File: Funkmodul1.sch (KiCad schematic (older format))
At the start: 14 parts, among them IC1 74HC4050, U1 ATMEGA128-16AU, Y1 Crystal_GND23

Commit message: Adds new submodules
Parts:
- removed IC1: 74HC4050, Housings_SSOP:SSOP-16_5.3x6.2mm_Pitch0.65mm, symbol 74HC4050
- removed R2, R3: R, Resistors_SMD:R_0603_HandSoldering, symbol R
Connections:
- net labels added: RX, TX
- net labels removed: +3V3, +5V, MISO, MOSI, SCK, SS
- wire segments 36 -> 23

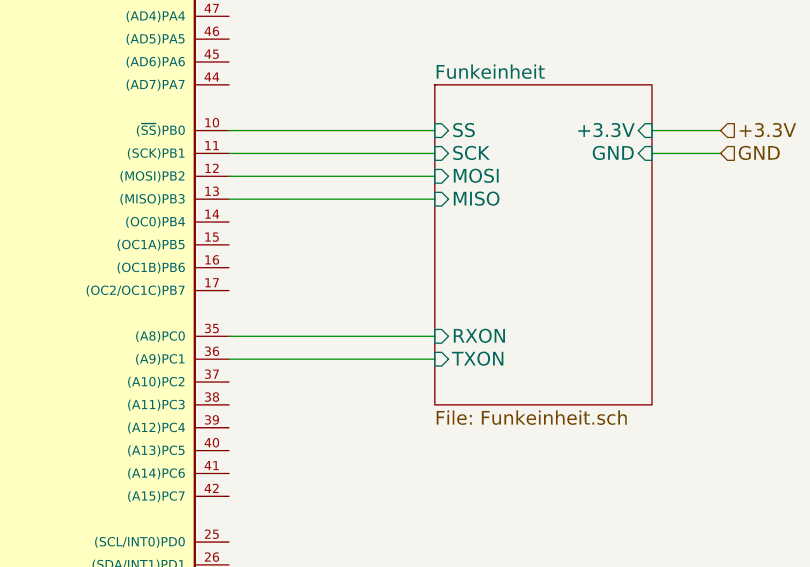
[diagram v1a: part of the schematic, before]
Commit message: Implements stepup dc/dc
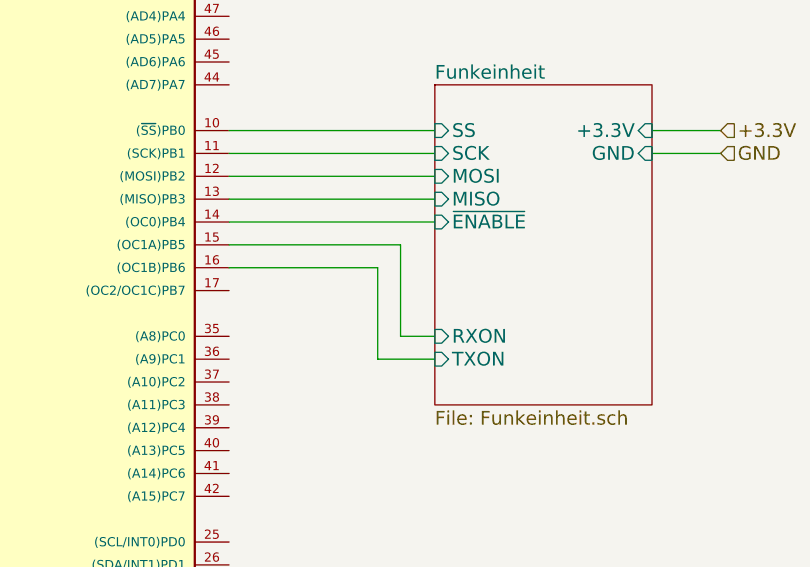
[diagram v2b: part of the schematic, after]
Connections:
- net Funkeinheit/RXON: now also U1.15 ((OC1A)PB5); no longer U1.35 ((A8)PC0)
- net Funkeinheit/TXON: now also U1.16 ((OC1B)PB6); no longer U1.36 ((A9)PC1)
- net Funkeinheit/~ENABLE~: now reaches U1.14 ((OC0)PB4)
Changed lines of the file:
@@
 LIBS:contrib
 LIBS:valves
+LIBS:nxp-ic
+LIBS:7400-ic
 LIBS:cubesatFunkmodul-cache
+LIBS:funkmodul
 EELAYER 25 0
 EELAYER END
@@
 U 1 1 59937F4F
 P 6850 3700
-AR Path="/5993797A/59937F4F" Ref="U1"  Part="1"
-AR Path="/5994EEB4/59937F4F" Ref="U2"  Part="1"
 F 0 "U1" H 5700 5600 50  0000 L BNN
 F 1 "ATMEGA128-16AU" H 7600 1750 50  0000 L BNN
@@
 U 1 1 59937F57
 P 6200 1300
-AR Path="/5993797A/59937F57" Ref="C4"  Part="1"
-AR Path="/5994EEB4/59937F57" Ref="C10"  Part="1"
 F 0 "C4" H 6225 1400 50  0000 L CNN
 F 1 "100nF" H 6225 1200 50  0000 L CNN
@@
 U 1 1 59937F5E
 P 6500 1300
-AR Path="/5993797A/59937F5E" Ref="C5"  Part="1"
-AR Path="/5994EEB4/59937F5E" Ref="C11"  Part="1"
 F 0 "C5" H 6525 1400 50  0000 L CNN
 F 1 "100nF" H 6525 1200 50  0000 L CNN
@@
 U 1 1 59937F89
 P 6850 1450
-AR Path="/5993797A/59937F89" Ref="L1"  Part="1"
-AR Path="/5994EEB4/59937F89" Ref="L2"  Part="1"
 F 0 "L1" V 6700 1475 50  0000 C CNN
 F 1 "10nH" V 7000 1450 50  0000 C CNN
@@
 U 1 1 59937F90
 P 7000 1250
-AR Path="/5993797A/59937F90" Ref="C6"  Part="1"
-AR Path="/5994EEB4/59937F90" Ref="C12"  Part="1"
 F 0 "C6" H 7025 1350 50  0000 L CNN
 F 1 "100nF" H 7025 1150 50  0000 L CNN
@@
 U 1 1 59937FF2
 P 5000 1850
-AR Path="/5993797A/59937FF2" Ref="R1"  Part="1"
-AR Path="/5994EEB4/59937FF2" Ref="R4"  Part="1"
 F 0 "R1" V 5080 1850 50  0000 C CNN
 F 1 "R" V 5000 1850 50  0000 C CNN
@@
 U 1 1 59938000
 P 5000 2200
-AR Path="/5993797A/59938000" Ref="C3"  Part="1"
-AR Path="/5994EEB4/59938000" Ref="C9"  Part="1"
 F 0 "C3" H 5025 2300 50  0000 L CNN
 F 1 "C" H 5025 2100 50  0000 L CNN
@@
 U 1 1 5993800E
 P 5250 1850
-AR Path="/5993797A/5993800E" Ref="D1"  Part="1"
-AR Path="/5994EEB4/5993800E" Ref="D2"  Part="1"
 F 0 "D1" H 5250 1950 50  0000 C CNN
 F 1 "D" H 5250 1750 50  0000 C CNN
@@
 U 1 1 5993801C
 P 3750 2650
-AR Path="/5993797A/5993801C" Ref="Y1"  Part="1"
-AR Path="/5994EEB4/5993801C" Ref="Y2"  Part="1"
 F 0 "Y1" H 3875 2850 50  0000 L CNN
 F 1 "Crystal_GND23" H 3875 2775 50  0000 L CNN
@@
 U 1 1 59938036
 P 4300 3200
-AR Path="/5993797A/59938036" Ref="C1"  Part="1"
-AR Path="/5994EEB4/59938036" Ref="C7"  Part="1"
 F 0 "C1" H 4325 3300 50  0000 L CNN
 F 1 "10pF" H 4325 3100 50  0000 L CNN
@@
 U 1 1 5993803D
 P 4550 2500
-AR Path="/5993797A/5993803D" Ref="C2"  Part="1"
-AR Path="/5994EEB4/5993803D" Ref="C8"  Part="1"
 F 0 "C2" H 4575 2600 50  0000 L CNN
 F 1 "10pF" H 4575 2400 50  0000 L CNN
@@
 F8 "TXON" I L 9050 3900 60
 F9 "+3.3V" I R 10000 2900 60
+F10 "~ENABLE~" I L 9050 3300 60
 $EndSheet
 Wire Wire Line
@@
 Wire Wire Line
 	8150 3200 9050 3200
-Wire Wire Line
-	8150 3800 9050 3800
-Wire Wire Line
-	8150 3900 9050 3900
 Text HLabel 10300 2900 2    60   Input ~ 0
 +3.3V
@@
 Wire Wire Line
 	5300 4800 5550 4800
+Wire Wire Line
+	9050 3300 8150 3300
+Wire Wire Line
+	9050 3800 8900 3800
+Wire Wire Line
+	8900 3800 8900 3400
+Wire Wire Line
+	8900 3400 8150 3400
+Wire Wire Line
+	9050 3900 8800 3900
+Wire Wire Line
+	8800 3900 8800 3500
+Wire Wire Line
+	8800 3500 8150 3500
 $EndSCHEMATC

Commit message: Adds new Modules and WDT Circuit
- Added Schematic for MAX892 Highside Switch
- Added Schematic for MC74HC4538A
- Constructed Watchdogtimer Circuit to Reset µC and Radiomodule
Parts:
- added C? (x2): C, symbol C
- added C? (x2): 1nF, symbol C
- added D?: D, symbol D
- added D?: D_Schottky, symbol D_Schottky
- added R?: 15k, symbol R
- added R? (x2): 100k, symbol R
- added R? (x2): 10k, symbol R
- added R? (x2): 100R, symbol R
- added U?: MAX892, symbol MAX892
- added U? (x2): MC74HC4538A, symbol MC74HC4538A
- C3: value C -> 10nF
- R1: value R -> 100k
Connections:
- net labels added: 3.3V, VCC, WDG_TRIGGER, ~ON~
- net labels removed: ATMEGA-RESET
- wire segments 28 -> 61
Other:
- note added: "min 50 mA, max 250mA\nR = 1.24*965/I_Lim"

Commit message: Adds ESD Protection and finalisation of wdt
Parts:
- removed R?: 100R, symbol R
- added C? (x2): 10µF, symbol C
- added C?: 100nF, symbol C
- added D? (x7): D, symbol D
- added Q?: Q_PNP_BCE, symbol Q_PNP_BCE
- added Q?: Q_NMOS_DGS, symbol Q_NMOS_DGS
- added R?: 47k, symbol R
- added R? (x4): 100k, symbol R
- added R?: 47R, symbol R
- added R?: 100R, symbol R
- added R? (x2): 10k, symbol R
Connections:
- net labels added: BURNWIRE, WIRE_CONN, ~MODULE_ON~
- wire segments 61 -> 88
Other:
- note added: "Burnwire circuit with detection"
- note added: "Watchdogtimer"
- note added: "switch for\nwatchdogtimer"

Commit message: Adds RFM23BP Module to Bib and Layout
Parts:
- removed C?: 1nF, symbol C
- removed D?: D_Schottky, symbol D_Schottky
- removed R?: 100k, symbol R
- R?: value 10k -> 100k
- R?: value 47k -> 22k
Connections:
- wire segments 88 -> 81
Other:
- note added: "ON Pulldown"
- moved on the sheet: R?
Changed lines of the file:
@@
 Connection ~ 4300 3050
 $Sheet
-S 9050 2700 950  1400
+S 9050 2700 950  1550
 U 5994BAF1
 F0 "Funkeinheit" 60
@@
 Connection ~ 1650 2650
 Wire Wire Line
-	2250 1250 2000 1250
+	2000 1250 2250 1250
 Text Label 2000 1250 0    60   ~ 0
 ~ON~
@@
 	2700 2400 3300 2400
 Wire Wire Line
-	2500 3600 3300 3600
-$Comp
-L C C?
-U 1 1 59B90241
-P 3450 3600
-F 0 "C?" H 3475 3700 50  0000 L CNN
-F 1 "1nF" H 3475 3500 50  0000 L CNN
-F 2 "" H 3488 3450 50  0001 C CNN
-F 3 "" H 3450 3600 50  0001 C CNN
-	1    3450 3600
-	0    1    1    0
-$EndComp
-Wire Wire Line
-	3300 3350 3200 3350
-Wire Wire Line
-	3200 3350 3200 3600
-Connection ~ 3200 3600
-Wire Wire Line
-	3600 3350 3750 3350
-Wire Wire Line
-	3750 3350 3750 3600
-Wire Wire Line
-	3600 3600 3850 3600
-Connection ~ 3750 3600
-Wire Wire Line
-	4150 3600 4150 3150
-Wire Wire Line
-	4150 3150 3300 3150
-Wire Wire Line
-	3300 3150 3300 1850
+	3300 1850 3300 3600
 Wire Wire Line
 	3300 1850 2400 1850
@@
 P 2250 1850
 F 0 "R?" V 2330 1850 50  0000 C CNN
-F 1 "10k" V 2250 1850 50  0000 C CNN
+F 1 "100k" V 2250 1850 50  0000 C CNN
 F 2 "" V 2180 1850 50  0001 C CNN
 F 3 "" H 2250 1850 50  0001 C CNN
 	1    2250 1850
-	0    1    1    0
-$EndComp
-$Comp
-L D_Schottky D?
-U 1 1 59B914FB
-P 4000 3600
-F 0 "D?" H 4000 3700 50  0000 C CNN
-F 1 "D_Schottky" H 4000 3500 50  0000 C CNN
-F 2 "" H 4000 3600 50  0001 C CNN
-F 3 "" H 4000 3600 50  0001 C CNN
-	1    4000 3600
-	1    0    0    -1
-$EndComp
-$Comp
-L R R?
-U 1 1 59B916C6
-P 3450 3350
-F 0 "R?" V 3530 3350 50  0000 C CNN
-F 1 "100k" V 3450 3350 50  0000 C CNN
-F 2 "" V 3380 3350 50  0001 C CNN
-F 3 "" H 3450 3350 50  0001 C CNN
-	1    3450 3350
 	0    1    1    0
 $EndComp
@@
 P 750 1500
 F 0 "R?" V 830 1500 50  0000 C CNN
-F 1 "47k" V 750 1500 50  0000 C CNN
+F 1 "22k" V 750 1500 50  0000 C CNN
 F 2 "" V 680 1500 50  0001 C CNN
 F 3 "" H 750 1500 50  0001 C CNN
@@
 L R R?
 U 1 1 59C31E7D
-P 2100 1400
-F 0 "R?" V 2180 1400 50  0000 C CNN
-F 1 "100k" V 2100 1400 50  0000 C CNN
-F 2 "" V 2030 1400 50  0001 C CNN
-F 3 "" H 2100 1400 50  0001 C CNN
-	1    2100 1400
+P 800 4700
+F 0 "R?" V 880 4700 50  0000 C CNN
+F 1 "100k" V 800 4700 50  0000 C CNN
+F 2 "" V 730 4700 50  0001 C CNN
+F 3 "" H 800 4700 50  0001 C CNN
+	1    800  4700
 	1    0    0    -1
 $EndComp
@@
 L GND #PWR?
 U 1 1 59C31F10
-P 2100 1550
-F 0 "#PWR?" H 2100 1300 50  0001 C CNN
-F 1 "GND" H 2100 1400 50  0000 C CNN
-F 2 "" H 2100 1550 50  0001 C CNN
-F 3 "" H 2100 1550 50  0001 C CNN
-	1    2100 1550
-	1    0    0    -1
-$EndComp
-Connection ~ 2100 1250
+P 800 4850
+F 0 "#PWR?" H 800 4600 50  0001 C CNN
+F 1 "GND" H 800 4700 50  0000 C CNN
+F 2 "" H 800 4850 50  0001 C CNN
+F 3 "" H 800 4850 50  0001 C CNN
+	1    800  4850
+	1    0    0    -1
+$EndComp
 Connection ~ 1000 2450
 Text HLabel 1000 2800 3    60   Input ~ 0
 ~MODULE_ON~
 Wire Wire Line
-	2100 1850 1300 1850
+	1300 1850 2100 1850
 Text HLabel 1150 1050 0    60   Input ~ 0
 3.3V
@@
 	1700 1700 3450 1700
 Wire Notes Line
-	3450 1700 3450 3150
-Wire Notes Line
-	3450 3150 4250 3150
-Wire Notes Line
-	4250 3150 4250 4300
-Wire Notes Line
-	4250 4300 1150 4300
+	3450 1700 3450 4300
 Wire Notes Line
 	1150 4300 1150 2600
@@
 	3650 5200 4050 5200
 Connection ~ 3950 5200
+Wire Wire Line
+	3300 3600 2500 3600
+Wire Notes Line
+	3450 4300 1150 4300
+Text Label 800  4550 0    60   ~ 0
+~ON~
+Wire Notes Line
+	550  4350 550  5200
+Wire Notes Line
+	550  5200 1100 5200
+Wire Notes Line
+	1100 5200 1100 4350
+Wire Notes Line
+	1100 4350 550  4350
+Text Notes 550  5300 0    60   ~ 0
+ON Pulldown
 $EndSCHEMATC

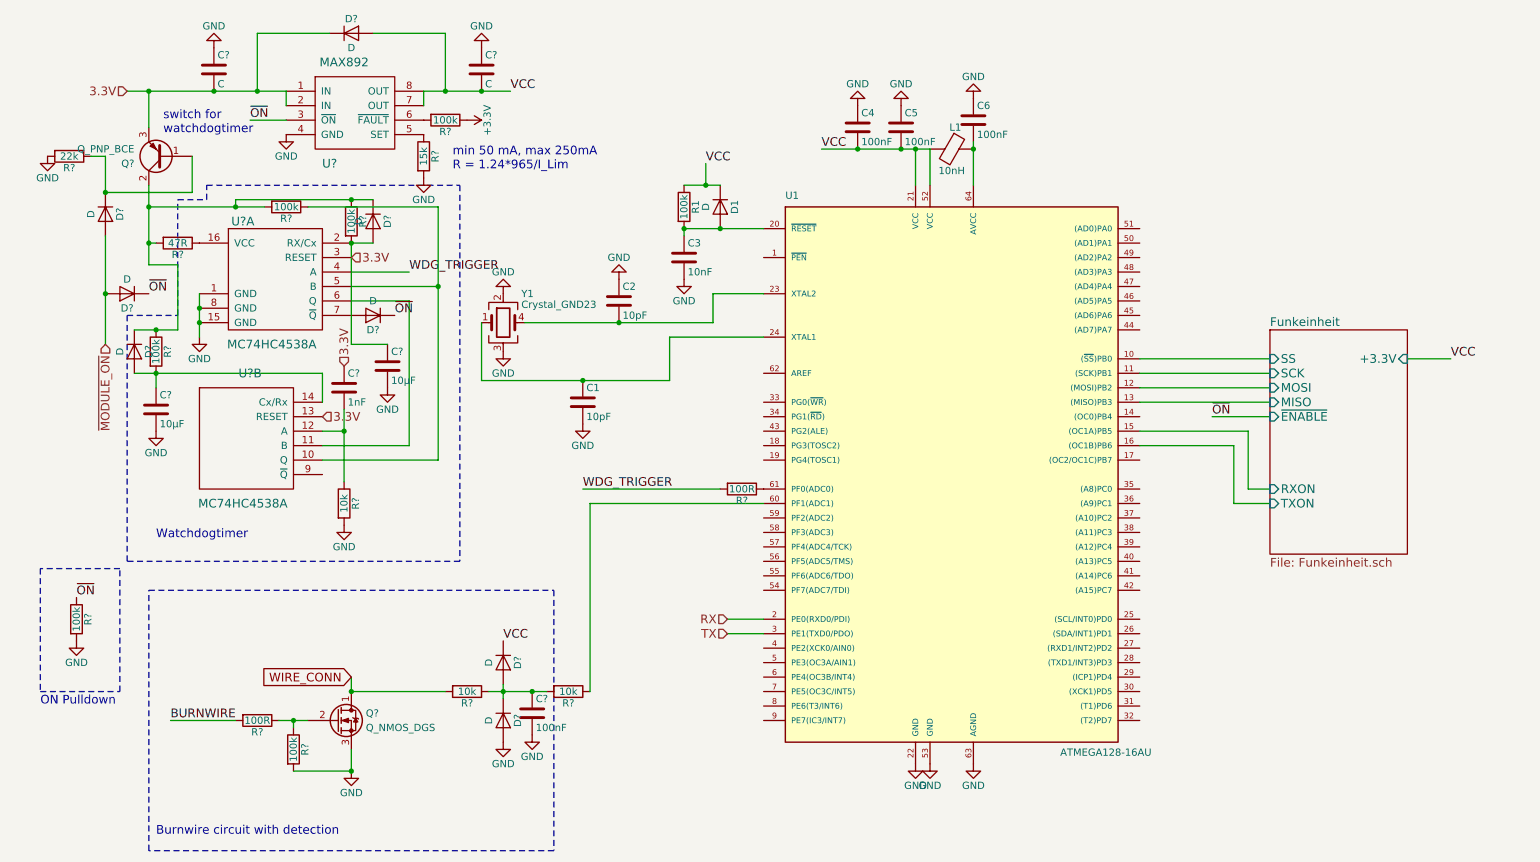
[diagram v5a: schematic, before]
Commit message: Adds component names
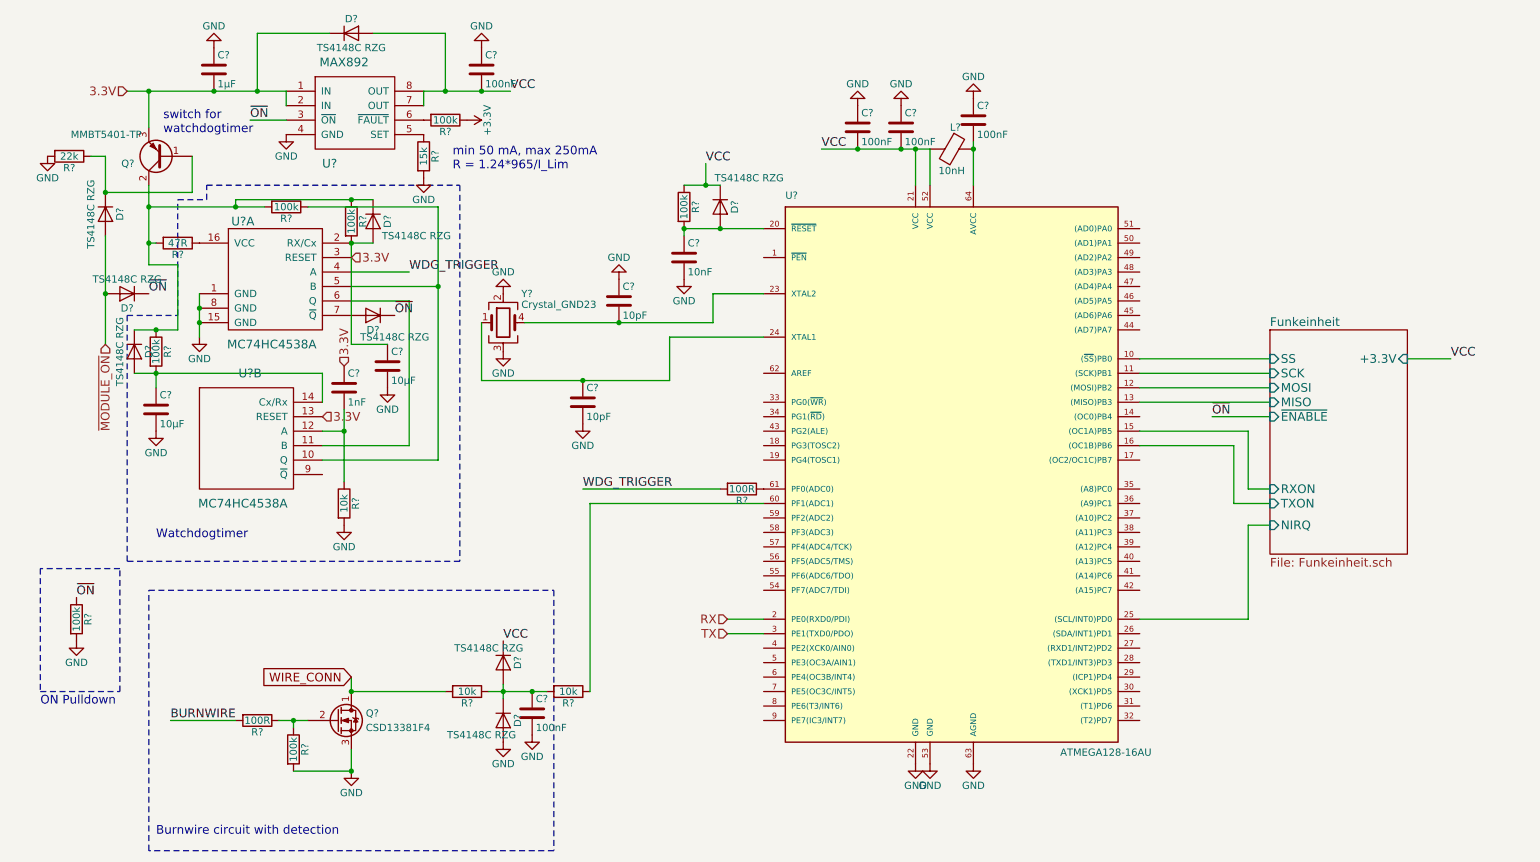
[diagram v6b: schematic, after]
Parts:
- C?: value C -> 100nF
- C?: value C -> 1µF
- C? (x2): footprint (none) -> Capacitors_SMD:C_0603_HandSoldering
- C? (x2): footprint (none) -> Capacitors_SMD:C_1210_HandSoldering
- D?: renamed from D1; value D -> TS4148C RZG
- D? (x8): value D -> TS4148C RZG; footprint (none) -> Diodes_SMD:D_0603
- Q?: value Q_PNP_BCE -> MMBT5401-TP
- Q?: value Q_NMOS_DGS -> CSD13381F4
- R? (x14): footprint (none) -> Resistors_SMD:R_0603_HandSoldering
- renumbered C4 to C?, C5 to C?, C6 to C?, C3 to C?, C1 to C?, C2 to C?, L1 to L?, R1 to R?, U1 to U?, Y1 to Y?
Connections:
- net Funkeinheit/NIRQ: now reaches U?.25 ((SCL/INT0)PD0)

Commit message: Change Diodes to  STTH102A
Datasheet: 
      http://www.st.com/content/ccc/resource/technical/document/datasheet/98/bc/9f/6f/26/c3/4e/73/CD00002613.pdf/files/CD00002613.pdf/jcr:content/translations/en.CD00002613.pdf
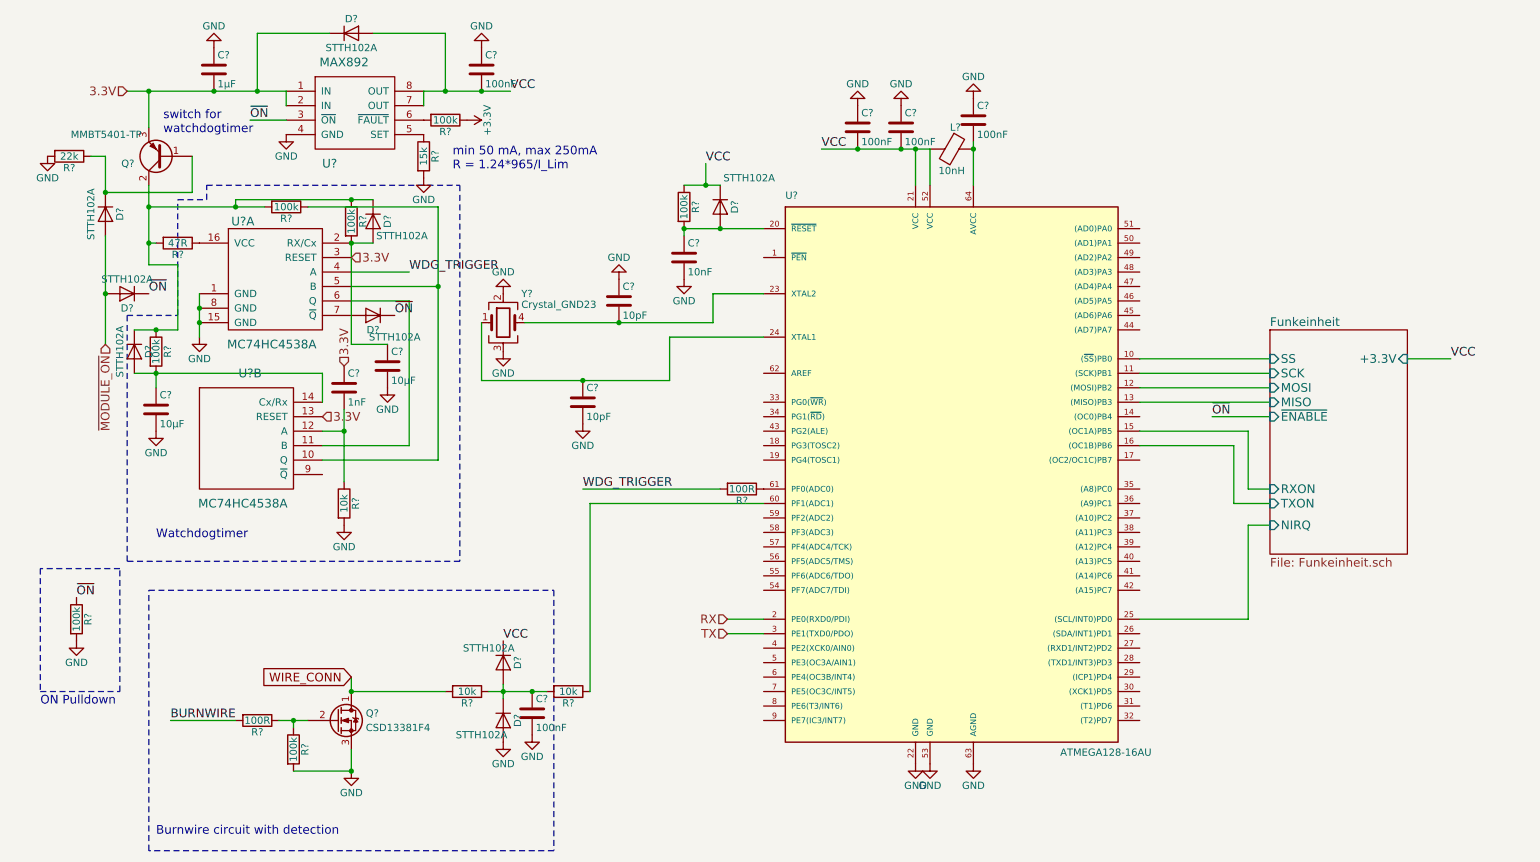
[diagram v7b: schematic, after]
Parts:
- D? (x9): value TS4148C RZG -> STTH102A
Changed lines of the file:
@@
 LIBS:contrib
 LIBS:valves
-LIBS:nxp-ic
-LIBS:7400-ic
 LIBS:cubesatFunkmodul-cache
 LIBS:funkmodul
@@
 P 5250 1850
 F 0 "D?" H 5250 1950 50  0000 C CNN
-F 1 "TS4148C RZG" V 5050 2050 50  0000 C CNN
+F 1 "STTH102A" V 5050 2050 50  0000 C CNN
 F 2 "Diodes_SMD:D_0603" H 5250 1850 50  0001 C CNN
 F 3 "" H 5250 1850 50  0001 C CNN
@@
 P 2700 650
 F 0 "D?" H 2700 750 50  0000 C CNN
-F 1 "TS4148C RZG" H 2700 550 50  0000 C CNN
+F 1 "STTH102A" H 2700 550 50  0000 C CNN
 F 2 "Diodes_SMD:D_0603" H 2700 650 50  0001 C CNN
 F 3 "" H 2700 650 50  0001 C CNN
@@
 P 1000 1900
 F 0 "D?" H 1000 2000 50  0000 C CNN
-F 1 "TS4148C RZG" H 1000 1800 50  0000 C CNN
+F 1 "STTH102A" H 1000 1800 50  0000 C CNN
 F 2 "Diodes_SMD:D_0603" H 1000 1900 50  0001 C CNN
 F 3 "" H 1000 1900 50  0001 C CNN
@@
 P 1150 2450
 F 0 "D?" H 1150 2550 50  0000 C CNN
-F 1 "TS4148C RZG" H 1150 2350 50  0000 C CNN
+F 1 "STTH102A" H 1150 2350 50  0000 C CNN
 F 2 "Diodes_SMD:D_0603" H 1150 2450 50  0001 C CNN
 F 3 "" H 1150 2450 50  0001 C CNN
@@
 P 2850 2600
 F 0 "D?" H 2850 2700 50  0000 C CNN
-F 1 "TS4148C RZG" H 2700 2750 50  0000 C CNN
+F 1 "STTH102A" H 2700 2750 50  0000 C CNN
 F 2 "Diodes_SMD:D_0603" H 2850 2600 50  0001 C CNN
-F 3 "" H 2850 2600 50  0001 C CNN
+F 3 "http://www.st.com/content/ccc/resource/technical/document/datasheet/98/bc/9f/6f/26/c3/4e/73/CD00002613.pdf/files/CD00002613.pdf/jcr:content/translations/en.CD00002613.pdf" H 2850 2600 50  0001 C CNN
 	1    2850 2600
 	-1   0    0    1
@@
 P 1200 2850
 F 0 "D?" H 1200 2950 50  0000 C CNN
-F 1 "TS4148C RZG" H 1200 2750 50  0000 C CNN
+F 1 "STTH102A" H 1200 2750 50  0000 C CNN
 F 2 "Diodes_SMD:D_0603" H 1200 2850 50  0001 C CNN
 F 3 "" H 1200 2850 50  0001 C CNN
@@
 P 2850 1950
 F 0 "D?" H 2850 2050 50  0000 C CNN
-F 1 "TS4148C RZG" V 2950 2250 50  0000 C CNN
+F 1 "STTH102A " V 2950 2150 50  0000 C CNN
 F 2 "Diodes_SMD:D_0603" H 2850 1950 50  0001 C CNN
-F 3 "" H 2850 1950 50  0001 C CNN
+F 3 "http://www.st.com/content/ccc/resource/technical/document/datasheet/98/bc/9f/6f/26/c3/4e/73/CD00002613.pdf/files/CD00002613.pdf/jcr:content/translations/en.CD00002613.pdf" H 2850 1950 50  0001 C CNN
 	1    2850 1950
 	0    1    1    0
@@
 P 3750 5400
 F 0 "D?" H 3750 5500 50  0000 C CNN
-F 1 "TS4148C RZG" V 3850 5250 50  0000 C CNN
+F 1 "STTH102A" V 3850 5250 50  0000 C CNN
 F 2 "Diodes_SMD:D_0603" H 3750 5400 50  0001 C CNN
 F 3 "" H 3750 5400 50  0001 C CNN
@@
 P 3750 5000
 F 0 "D?" H 3750 5100 50  0000 C CNN
-F 1 "TS4148C RZG" V 3650 4900 50  0000 C CNN
+F 1 "STTH102A" V 3650 4900 50  0000 C CNN
 F 2 "Diodes_SMD:D_0603" H 3750 5000 50  0001 C CNN
 F 3 "" H 3750 5000 50  0001 C CNN
